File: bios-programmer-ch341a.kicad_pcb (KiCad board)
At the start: 2 copper layers, 50 x 56 mm, 47 parts, among them J1 USB_B_Micro, J4 -Banana-, J5 +Banana+, J6 ZIF16, J7 Conn_02x04_Counter_Clockwise, J8 Conn_02x04_Counter_Clockwise, Q1 SSM3J328R, Q2 SSM3J328R, Q3 SSM3J328R, Q4 SSM3J328R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

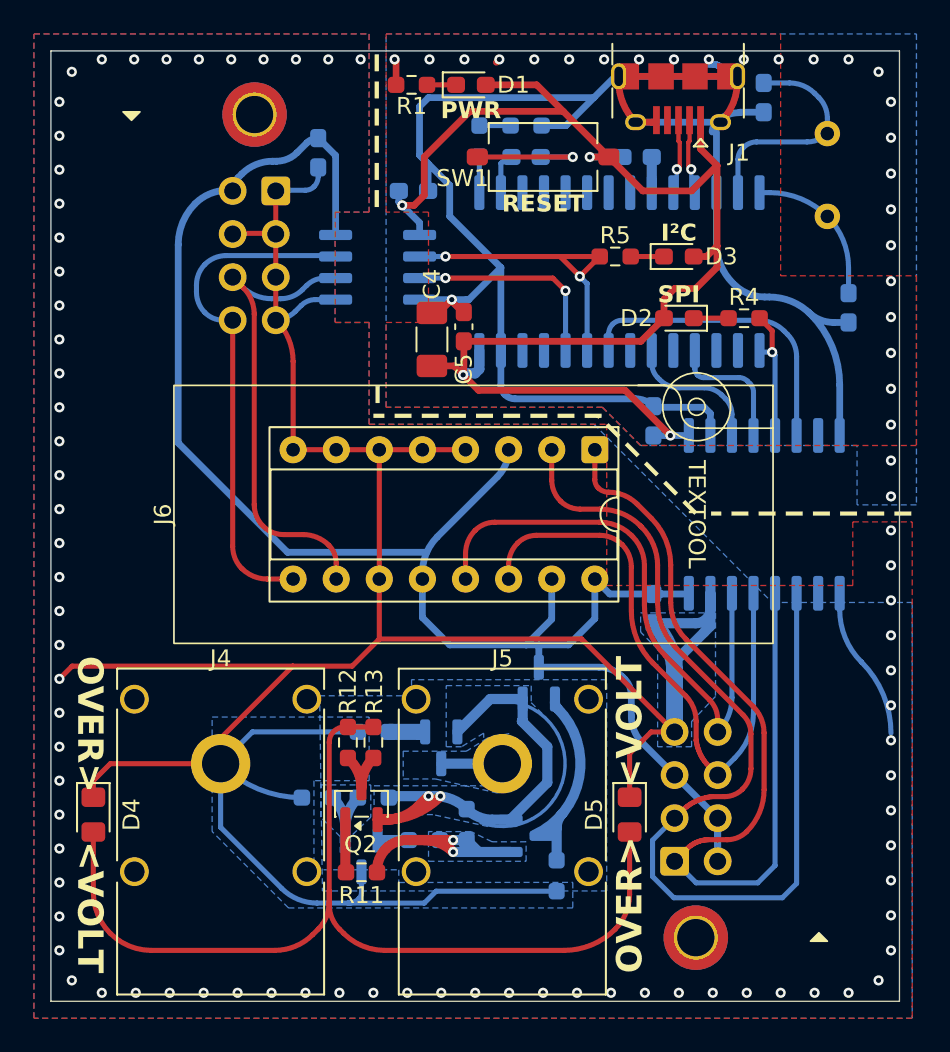
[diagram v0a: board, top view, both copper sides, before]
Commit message: SCH/PCB: adding sense wires & some beautification
Rationale: sense wires are not strictly necessary and the design would work
perfectly without. It does however add some indication of the voltage as it is
present on the IC under program through the IDC connectors. It is after all an
unknown how long and thick the wires leading up to this IC are.
That said, it wouldn't provide any insight in any voltage drop on the actual
data lines and as such provide less information than really required.

The routing, with one sense pair on the bottom and one on top is a result of
requiring the same pinout on both IDC connectors. It is reasonable to expect
that the IDC to clip 'adapter' can be used on both sides of the board.
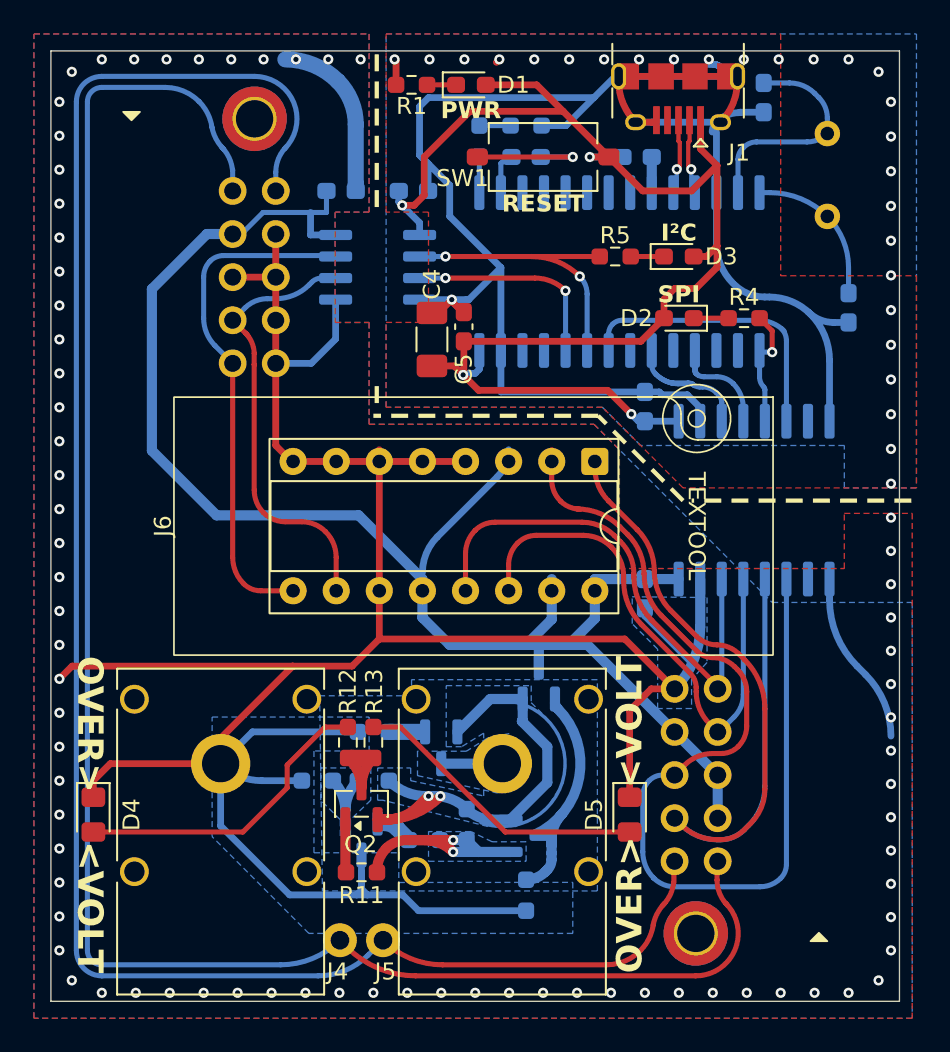
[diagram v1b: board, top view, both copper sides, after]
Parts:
- added J9: SENSE, TerminalBlock_TE-Connectivity:TerminalBlock_TE_282834-2_1x02_P2.54mm_Horizontal, B.Cu at (60.6, 82.4)
- J7, J8: value Conn_02x04_Counter_Clockwise -> Conn_02x05_Odd_Even; footprint Connector_IDC:IDC-Header_2x04_P2.54mm_Horizontal -> footprints:IDC-Header_2x05_P2.54mm_Horizontal_1.64mm_pad
- moved C10 2.62 mm to (58.1, 38.2), turned to 0 degrees
- moved R14 2.14 mm to (69.0, 79.8)
- moved U2 1.03 mm to (82.4, 56.5)
- moved C9 1.01 mm to (76.0, 62.0)
- moved R7 1.00 mm to (60.0, 73.0)
- moved R8 1.00 mm to (56.7, 73.0)
- moved U4 1.00 mm to (59.3, 76.4)
- moved C8 0.98 mm to (76.0, 51.0)
- moved J6 0.69 mm to (73.0, 54.2)
- moved H1 0.25 mm to (53.0, 34.0)
- moved H2 0.25 mm to (79.0, 82.0)
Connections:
- D4 pad 2: /OVPLED -> Net-(D4-A)
- D5 pad 2: /OVPLED -> Net-(D5-A)
- J7 pad 1: /CS_I -> /SNS+
- J7 pad 2: VDD -> /SNS-
- J7 pad 3: /MISO_I -> /CS_I
- J7 pad 5: VDD -> /MISO_I
- J7 pad 6: /CLK_I -> VDD
- J7 pad 7: GNDD -> VDD
- J7 pad 8: /MOSI_I -> /CLK_I
- J8 pad 1: GNDD -> /SNS+
- J8 pad 2: VDD -> /SNS-
- J8 pad 4: GNDD -> VDD
- J8 pad 6: /SCL_I -> GNDD
- J8 pad 8: /SDA_I -> /SCL_I
- R12 pad 1: /OVPLED -> Net-(D4-A)
- R13 pad 2: /OVPLED -> Net-(D5-A)
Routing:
- net /SNS+: track 0.00 -> 100.7 mm
- net /SNS-: track 0.00 -> 100.0 mm
- net /OVPLED: track 58.9 -> 0.00 mm
- net Net-(D4-A): track 0.00 -> 18.3 mm
- net Net-(D5-A): track 0.00 -> 17.7 mm
- net VDD: track 104.2 -> 94.7 mm
- net /MOSI_I: track 34.9 -> 28.5 mm
- net /CS_I: track 54.8 -> 49.1 mm
- net /CLK_I: track 35.5 -> 30.5 mm
- net GND: track 223.7 -> 219.5 mm
- net /VG_MAIN: track 11.8 -> 14.5 mm
- net /SCL_I: track 27.6 -> 25.5 mm
- net VBUS: track 86.2 -> 84.2 mm
- net GNDD: track 469.3 -> 471.1 mm, vias 74 -> 75
- net /CLK: track 7.84 -> 6.79 mm
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
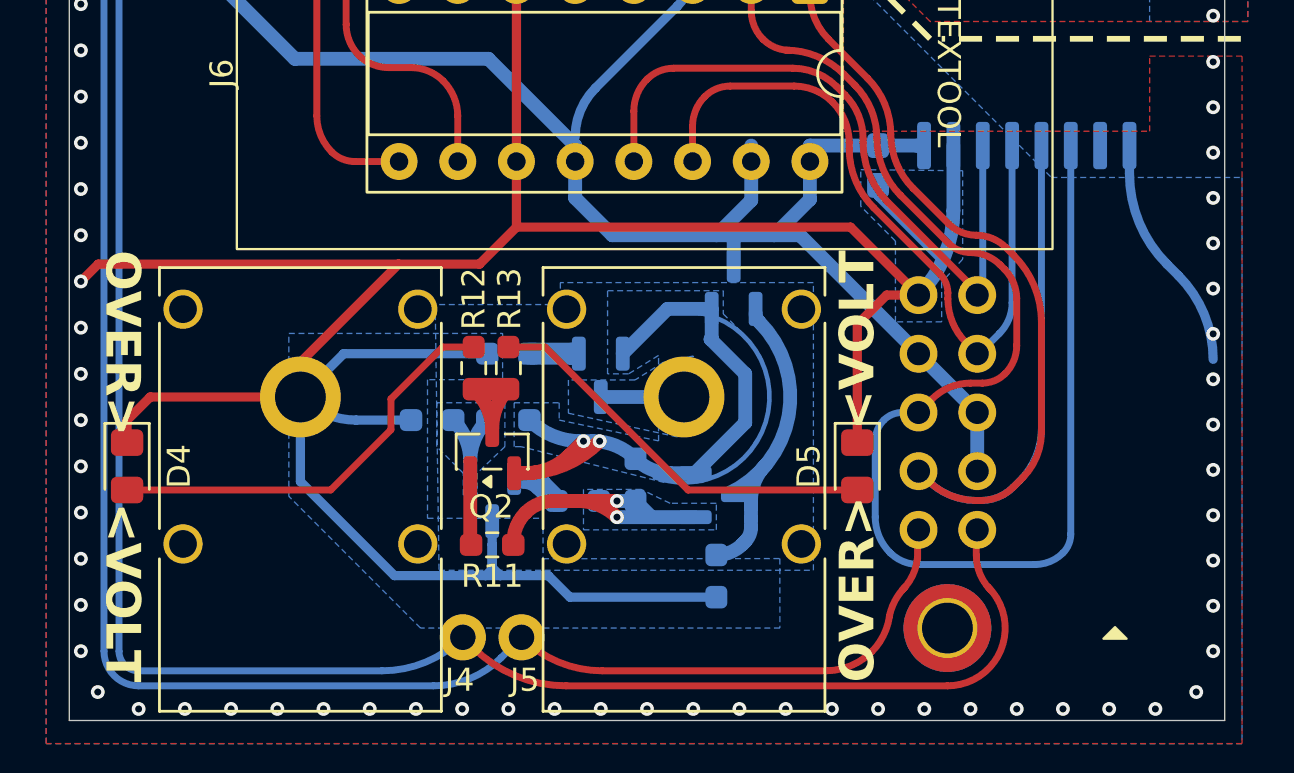
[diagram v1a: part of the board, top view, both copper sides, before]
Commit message: PCB: additional LED resistor
Previously having 2 resistors in parallel, leading to 2 parallel LEDs could
potentially lead to an issue in case any of the LEDs fails or burns out. The
other remaining LED would then have to bear all of the current and surely burn
out as well.

Note that the LEDs are already potentially overdriven, depening on the input
voltage. That said, no more than 8V is supported for the power protection path
anyway.
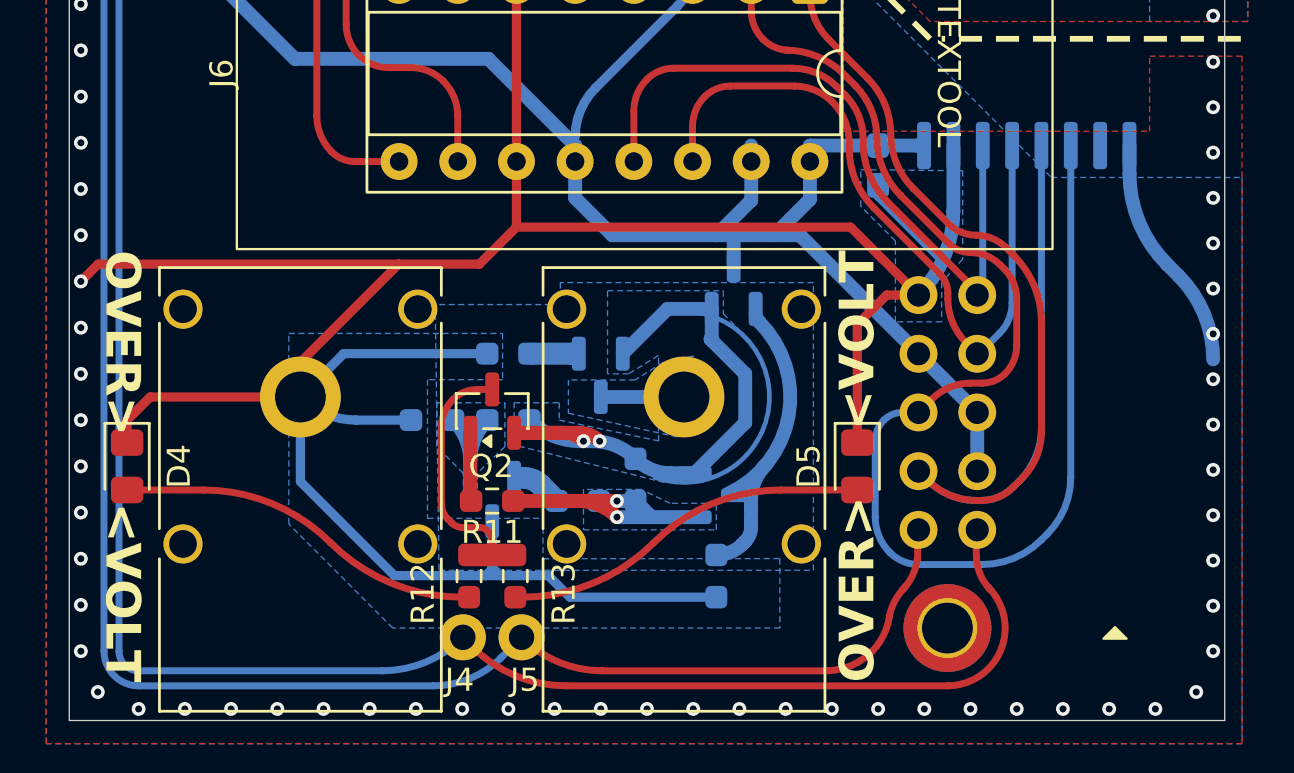
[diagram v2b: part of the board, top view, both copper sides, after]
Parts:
- moved R13 9.00 mm to (60.3, 79.8), turned to -90 degrees
- moved R12 9.00 mm to (58.3, 79.8), turned to 90 degrees
- moved R11 1.90 mm to (59.3, 76.5)
- moved Q2 1.75 mm to (59.3, 72.6)
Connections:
- net /Q2_S renamed Net-(Q2-D)
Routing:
- net Net-(Q2-D): track 4.68 -> 11.7 mm
- net Net-(D4-A): track 18.3 -> 15.7 mm
- net Net-(D5-A): track 17.7 -> 15.7 mm
- net /MISO_I: track 60.9 -> 59.8 mm
- net /VSW: track 28.5 -> 27.9 mm

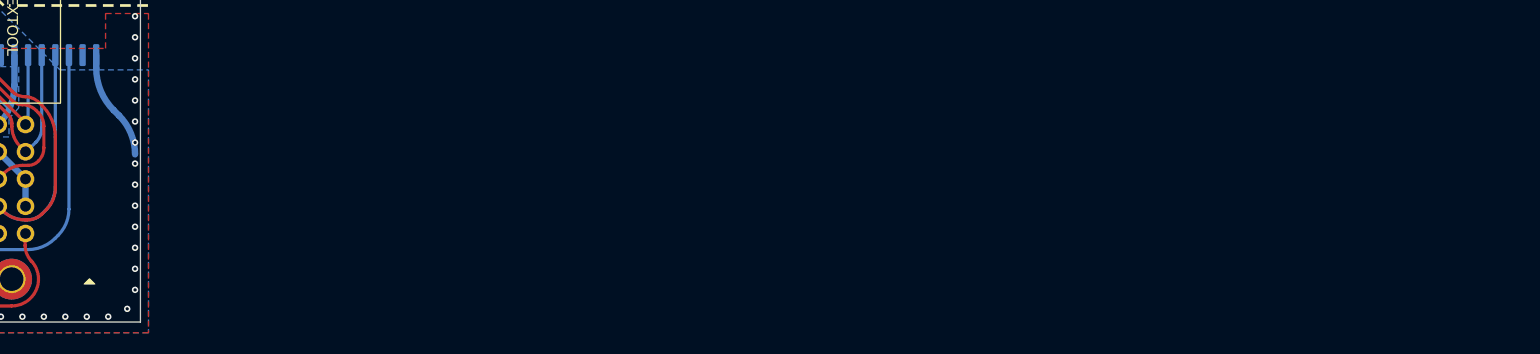
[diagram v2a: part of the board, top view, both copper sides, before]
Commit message: pcb: silkscreens; 50x40 mil text 8mil (auto) thickness
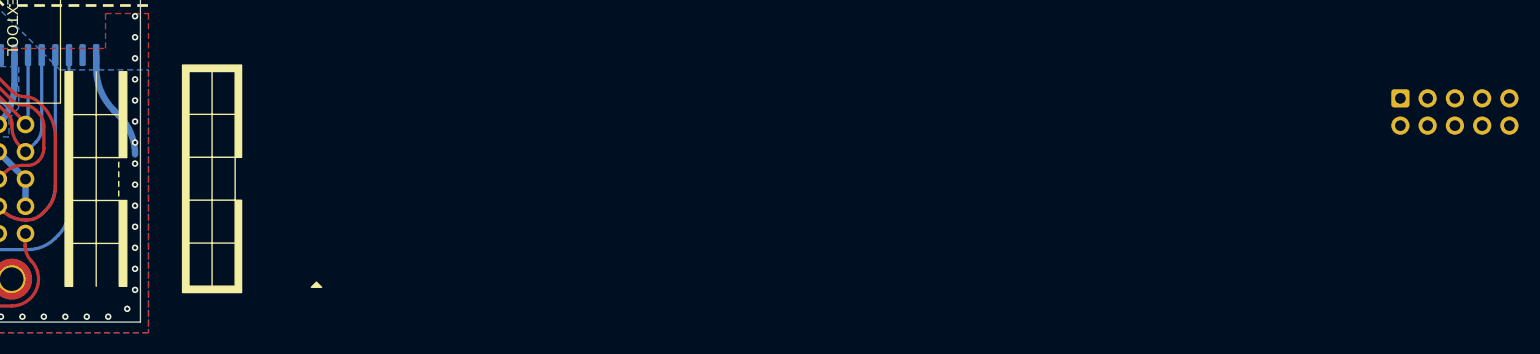
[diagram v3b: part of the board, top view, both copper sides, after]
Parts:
- added REF**: IDC-Header_2x05_P2.54mm_Horizontal, Connector_IDC:IDC-Header_2x05_P2.54mm_Horizontal, B.Cu at (208.4, 65.2)

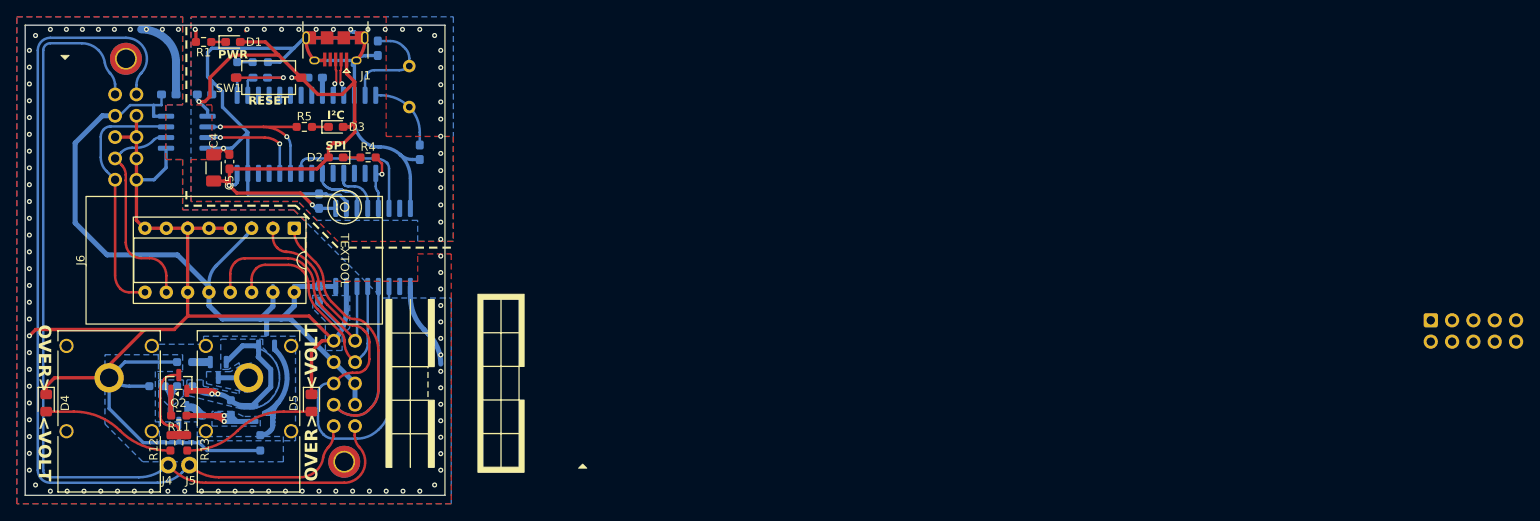
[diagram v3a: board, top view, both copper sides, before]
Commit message: PCB: silkscreen connector layouts
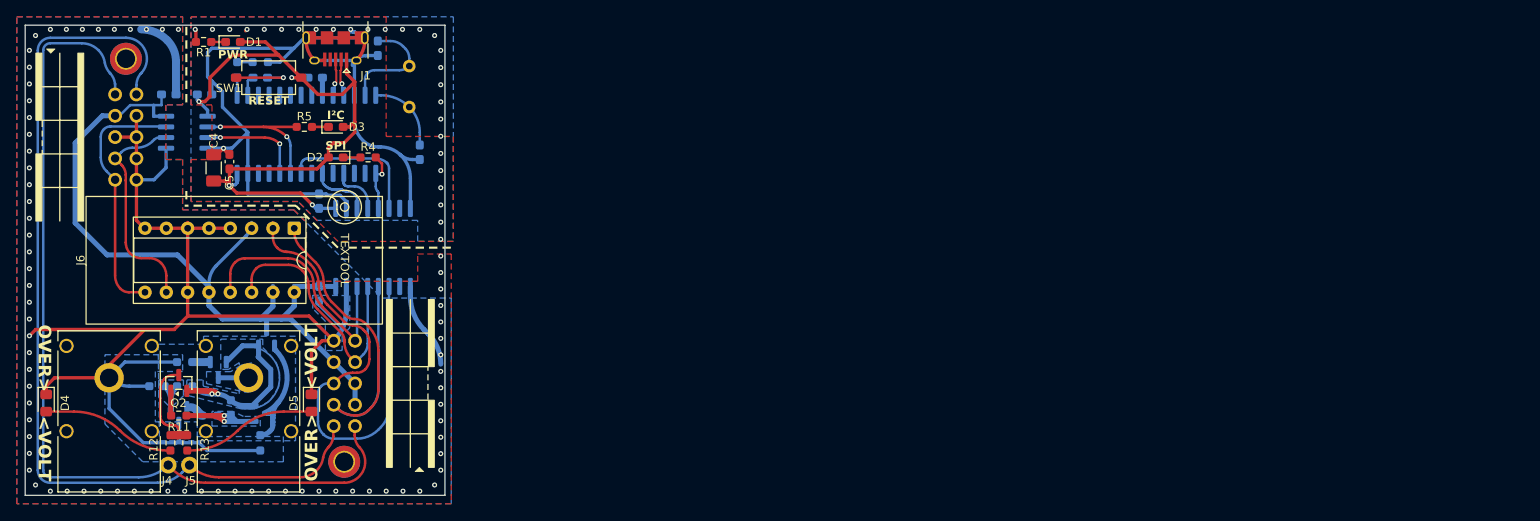
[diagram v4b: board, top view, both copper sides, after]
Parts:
- removed REF**: IDC-Header_2x05_P2.54mm_Horizontal, Connector_IDC:IDC-Header_2x05_P2.54mm_Horizontal

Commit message: silkscreen table + some improvements
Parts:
- removed C5: 100nF, Capacitor_SMD:C_0603_1608Metric_Pad1.08x0.95mm_HandSolder
- C4: moved to B.Cu
- moved C4 0.79 mm to (63.0, 47.6), turned to 180 degrees
- moved C8 0.75 mm to (76.0, 51.7)
- moved C10 0.25 mm to (58.4, 38.2)
- moved R12 0.25 mm to (58.3, 79.5)
- moved R13 0.25 mm to (60.3, 79.5)
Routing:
- net VBUS: track 84.2 -> 76.0 mm
- net GND: track 219.5 -> 223.5 mm, vias 28 -> 27
- net Net-(D5-A): track 15.7 -> 16.7 mm
- net Net-(D4-A): track 15.7 -> 16.7 mm

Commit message: pcb silkscreen reference font Inconsolata
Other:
- board text added: "ABCDEFGHIJKLM NOPQRSTUVWXYZ"

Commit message: pcb silkscreen Anonymous Pro text disregard kicad check for TT  font width; kicd font is thinner and not detected
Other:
- board text removed: "ABCDEFGHIJKLM NOPQRSTUVWXYZ"

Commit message: PCB: silkscreen in metric & font taller than wide
I think it looks kinda good with a much taller than wide font.

Text boxes were replaced with text components which are much easier to position
as intented. It is still difficult to get good text positioning/sizing in Kicad
and having separate components works around this.
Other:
- board text added: "A0"
- board text added: "A1"
- board text added: "A2"
- board text added: "CLK"
- board text added: "CS"
- board text added: "GND"
- board text added: "MISO"
- board text added: "MOSI"
- board text added: "SCL"
- board text added: "SDA"
- board text added: "SNS+"
- board text added: "SNS-"
- board text added: "VCC"
- board text added: "WP"
- board text added: "~RST"
- board text added: "~WP"
